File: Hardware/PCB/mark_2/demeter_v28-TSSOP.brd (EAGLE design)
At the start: 90 x 56 mm, 69 parts, among them IC1 4050, IC2 LM1117-5.0, IC3 LM1117-3.3, IC4 XBEE, IC5 MCP3424, IC6 MCP23017SO, IC8 ATMEGA32U4-AU, Q1 IRLML6402, Q3 IRLML6402, Q5 IRLML6402, X2 POWER

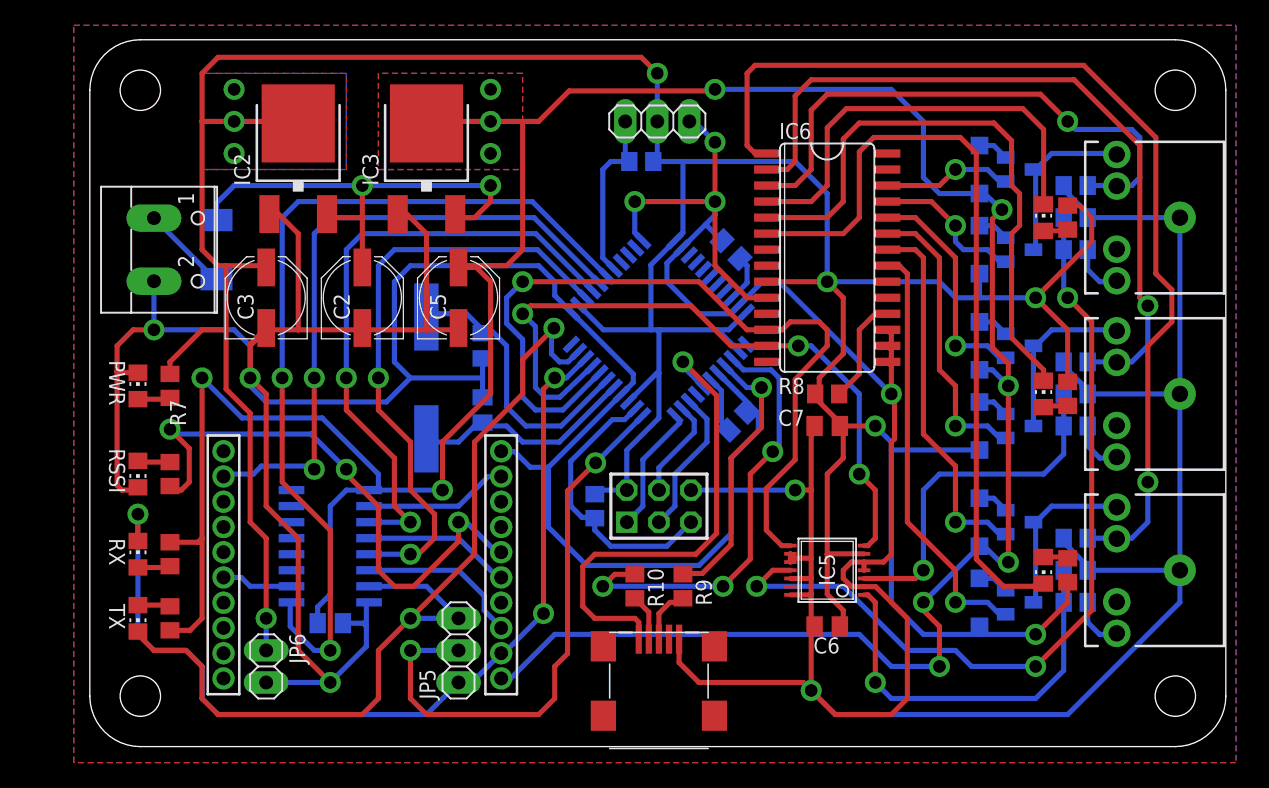
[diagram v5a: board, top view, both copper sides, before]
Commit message: 
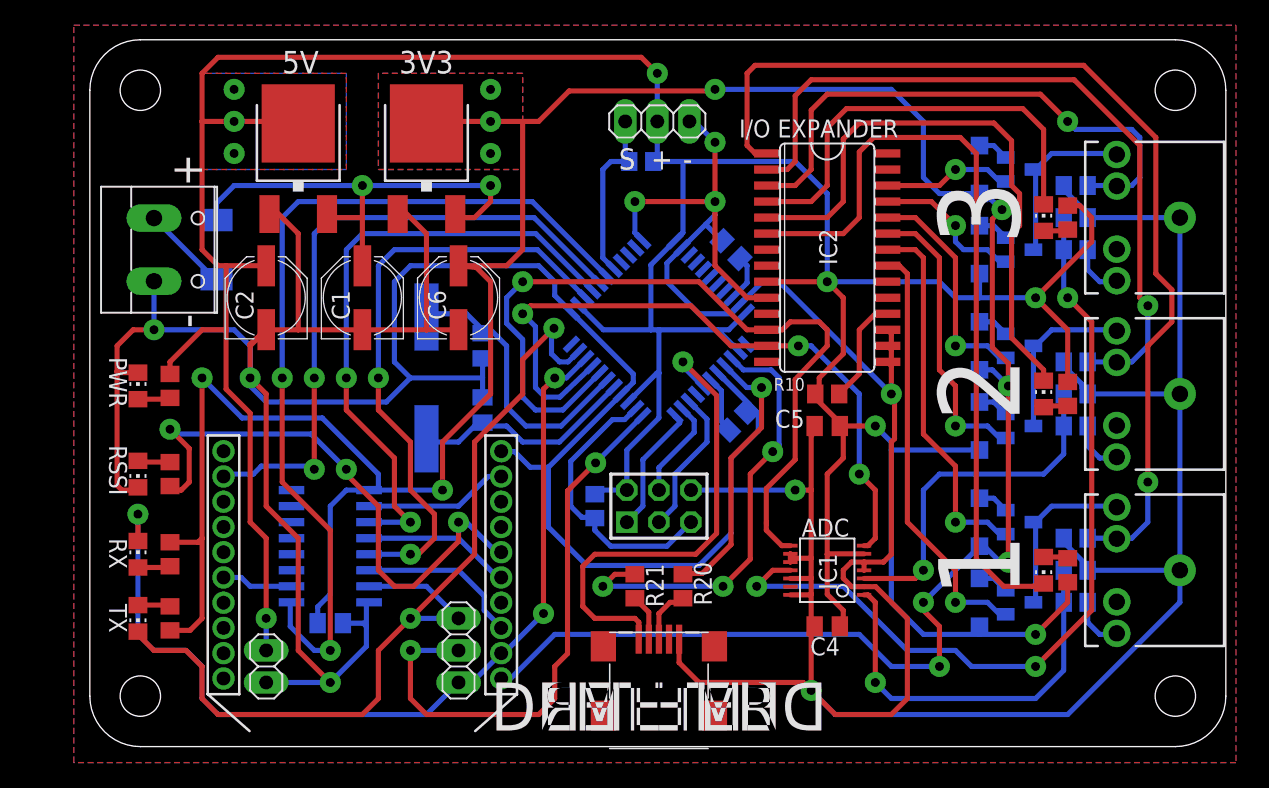
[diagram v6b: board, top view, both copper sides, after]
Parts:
- removed C11: 100nF, mark_2:C0805K
- removed JP5: (no value), mark_2:1X03
- removed JP6: (no value), mark_2:1X02
- removed R22: 1k, mark_2:R0805
- added C4: 100nF, mark_2:C0805K
- added JP3: (no value), mark_2:1X03
- added JP4: AVR-ISP, mark_2:AVR-ISP-6
- added R2: 1k5, mark_2:R0805
- C1: value 1uF -> 22uF; device mark_2:C0805K -> mark_2:PANASONIC_D
- C2: value 22uF -> 100uF
- C3, C5: value 100uF -> 100nF; device mark_2:PANASONIC_D -> mark_2:C0805K
- C6: value 100nF -> 100uF; device mark_2:C0805K -> mark_2:PANASONIC_D
- C7: value 100nF -> 1uF
- D1: value S1M -> (none); device mark_2:DO-214AC -> mark_2:SOD123
- D7: value (none) -> S1M; device mark_2:SOD123 -> mark_2:DO-214AC
- IC1: value 4050 -> MCP3424; device mark_2:SO16 -> mark_2:TSSOP14
- IC2: value LM1117-5.0 -> MCP23017; device mark_2:DPACK -> mark_2:SO28W
- IC3: value LM1117-3.3 -> LM1117-5.0
- IC4: value XBEE -> LM1117-3.3; device mark_2:XBEE-1 -> mark_2:DPACK
- IC5: value MCP3424 -> 4050; device mark_2:TSSOP14 -> mark_2:SO16
- IC6: value MCP23017SO -> XBEE; device mark_2:SO28W -> mark_2:XBEE-1
- IC7: value ATMEGA32U4-AU -> ATMEGA32U4
- JP1: value AVR-ISP -> (none); device mark_2:AVR-ISP-6 -> mark_2:1X03
- JP2: device mark_2:1X03 -> mark_2:1X02
- R1, R19, R7: value 1k -> 10k
- R10: value 22 -> 10k
- R13, R15: value 1k5 -> 1k
- R18: value 1k5 -> 10k
- R20: value 10k -> 22
- R21: value 1k -> 22
- R3, R6: value 10k -> 1k
- R5, R8: value 10k -> 1k5
- R9: value 22 -> 1k
- moved R17 74.6 mm to (6.35, 21.6), flipped to the top, turned to 270 degrees
- moved R7 73.5 mm to (78.1, 44.5), flipped to the bottom, turned to 180 degrees
- moved R15 73.4 mm to (6.35, 10.2), flipped to the top, turned to 270 degrees
- moved R14 73.2 mm to (6.35, 28.6), flipped to the top, turned to 90 degrees
- moved R16 72.9 mm to (6.35, 15.2), flipped to the top, turned to 90 degrees
- moved R1 71.9 mm to (78.1, 16.5), flipped to the bottom, turned to 180 degrees
- moved D1 66.6 mm to (70.5, 11.4)
- moved D7 60.8 mm to (10.0, 39.4)
- moved JP2 53.1 mm to (14.0, 6.35), turned to 270 degrees
- moved R18 43.2 mm to (40.0, 19.1), turned to 90 degrees
- moved R9 42.7 mm to (78.1, 41.9), flipped to the bottom, turned to 180 degrees
- moved IC2 42.6 mm to (58.4, 39.4), turned to 270 degrees
- moved IC1 39.4 mm to (58.4, 14.0), flipped to the top, turned to 90 degrees
- moved IC5 39.4 mm to (19.1, 15.9), flipped to the bottom, turned to 270 degrees
- moved IC6 39.4 mm to (21.6, 25.4), turned to 180 degrees
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- renumbered IC8 to IC7, Q9 to K1, X2 to X1
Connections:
- removed net N$23 (its old number): PWR3.A, R19.1
- new net N$5: PWR3.A, R13.1
- net +12V: now also C1.+, D7.C, IC4.3; no longer C2.+, D1.C, IC2.3
- net +3V3: now also C3.1, C6.+, D2.A, D4.A, D6.A, IC4.4, IC5.1, IC6.1, R15.2, R16.2; no longer C11.1, C5.+, D3.A, D5.A, D7.A, IC1.1, IC3.4, IC4.1, R21.2, R22.2
- net +5V: now also C2.+, C4.1, C5.1, D1.A, D3.A, D5.A, IC1.6, IC2.9, IC3.4, JP2.1, JP3.2, JP4.2, R10.2, R13.2, R14.2, R18.2; no longer C3.+, C6.1, C7.1, D2.A, D4.A, D6.A, IC2.4, IC5.6, IC6.9, JP1.2, JP2.2, JP6.1, R20.2, R3.2, R7.2, R8.2
- net CH1: now also IC1.1, R2.1, R3.1; no longer IC5.1, R13.1, R14.1
- net CH2: now also IC1.3, R5.1, R6.1; no longer IC5.3, R15.1, R16.1
- net CH3: now also IC1.11, R8.1, R9.1; no longer IC5.11, R17.1, R18.1
- net CTS: now also IC6.12; no longer IC4.12
- net D+: now also R20.1; no longer R9.1
- net D-: now also R21.1; no longer R10.1
- net DATA: now also JP3.1, R19.1; no longer JP2.1, R20.1
- net DTR: now also IC5.3; no longer IC1.3
- net EN: now also JP1.2; no longer JP5.2
- net EN1-3: now also IC2.22; no longer IC6.22
- net EN1-5: now also IC2.21; no longer IC6.21
- net EN2-3: now also IC2.24; no longer IC6.24
- net EN2-5: now also IC2.23; no longer IC6.23
- net EN3-3: now also IC2.26; no longer IC6.26
- net EN3-5: now also IC2.25; no longer IC6.25
- net GND: now also C1.-, C3.2, C4.2, C5.2, C6.-, IC1.10, IC1.12, IC1.14, IC1.2, IC1.4, IC1.5, IC1.9, IC2.10, IC2.15, IC2.16, IC2.17, IC4.1, IC5.8, JP2.2, JP3.3, JP4.6, R1.1, R3.2, R6.2, R7.1, R9.2; no longer C1.2, C11.2, C3.-, C5.-, C6.2, IC1.8, IC2.1, IC4.10, IC5.10, IC5.12, IC5.14, IC5.2, IC5.4, IC5.5, IC5.9, IC6.15, IC6.16, IC6.17, JP1.6, JP2.3, JP6.2, R14.2, R16.2, R17.2, R5.1, R6.1
- net MISO: now also JP4.1; no longer JP1.1
- net MOSI: now also JP4.4; no longer JP1.4
- net N$1: now also D7.A; no longer D1.A
- net N$10: now also IC2.4, PWR1.C; no longer IC6.4, PWR3.C
- net N$11: now also IC2.18, R10.1; no longer IC6.18, R8.1
- net N$13: now also D1.C; no longer D2.C
- net N$14: now also D2.C; no longer D3.C
- net N$16: now also D3.C; no longer D4.C
- net N$17: now also D4.C; no longer D5.C
- net N$19: now also D5.C; no longer D6.C
- net N$2: now also R14.1; no longer R7.1
- net N$20: now also D6.C; no longer D7.C
- net N$24: now also C7.1; no longer C1.1
- net N$28: now also R20.2; no longer R9.2
- net N$29: now also R21.2; no longer R10.2
- net N$3: now also IC5.6, IC6.3; no longer IC1.6, IC4.3
- net N$30: now also R2.2; no longer R13.2
- net N$32: now also R5.2; no longer R15.2
- net N$33: now also IC2.5; no longer IC6.5
- net N$34: now also R8.2; no longer R18.2
- net N$36: now also R15.1; no longer R21.1
- net N$37: now also R16.1; no longer R22.1
- net N$4: now also IC5.4, IC6.5; no longer IC1.4, IC4.5
- net N$6: now also R17.1; no longer R1.1
- net N$7: now also IC5.2, IC6.9; no longer IC1.2, IC4.9
- net N$8: now also IC5.10, IC6.16; no longer IC1.10, IC4.16
- net N$9: now also IC2.6, PWR3.C; no longer IC6.6, PWR1.C
- net RESET: now also IC5.5; no longer IC1.5
- net RSSI: now also IC6.6, R17.2; no longer IC4.6, R1.2
- net RST: now also JP4.5, R18.1; no longer JP1.5, R3.1
- net RTS: now also IC5.9; no longer IC1.9
- net RX: now also IC6.2, JP1.1; no longer IC4.2, JP5.1
- net SCK: now also JP4.3; no longer JP1.3
- net SCL: now also IC1.8, IC2.12; no longer IC5.8, IC6.12
- net SDA: now also IC1.7, IC2.13; no longer IC5.7, IC6.13
- net SN1: now also IC2.1, R1.2; no longer IC6.1, R4.2
- net SN2: now also IC2.2, R4.2; no longer IC6.2, R5.2
- net SN3: now also IC2.3, R7.2; no longer IC6.3, R6.2
- net TX: now also IC5.7, JP1.3; no longer IC1.7, JP5.3
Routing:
- net N$23 (its old number): track 2.36 -> 0.00 mm
- net N$5: track 0.00 -> 1.95 mm
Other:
- board text added: "+"
- board text added: "-"
- board text added: "1"
- board text added: "2"
- board text added: "3"
- board text added: "3V3"
- board text added: "5V"
- board text added: "ADC"
- board text added: "DEMETER"
- board text added: "I/O EXPANDER"
- board text added: "S"
